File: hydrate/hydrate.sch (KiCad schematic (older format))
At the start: 1 part, among them U1 K32L2Bx1VFM0A

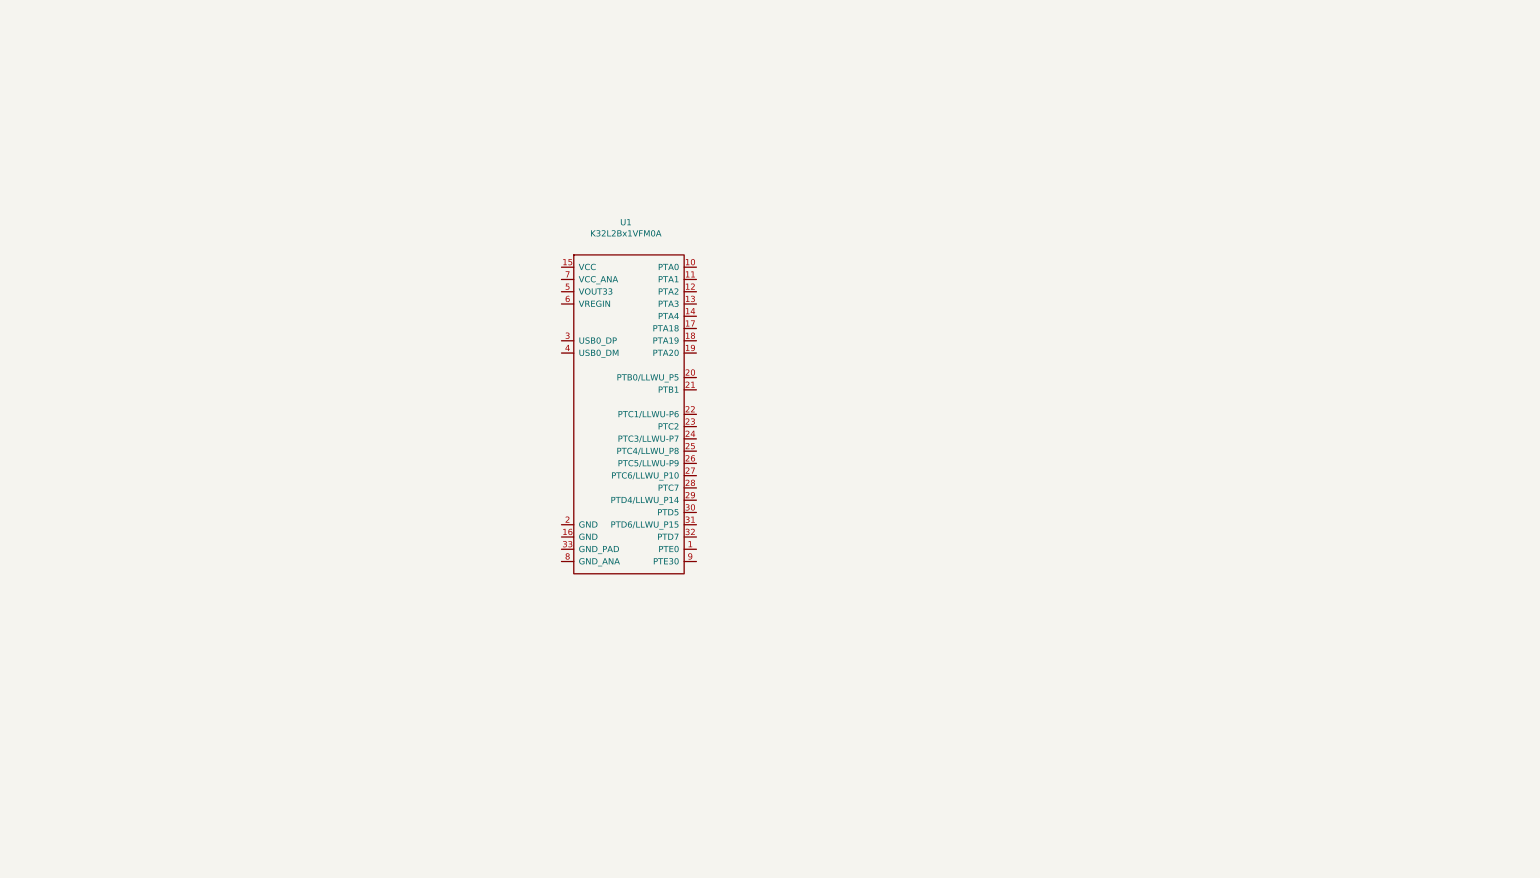
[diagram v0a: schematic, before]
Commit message: Saving place. MCU and power management ICs added
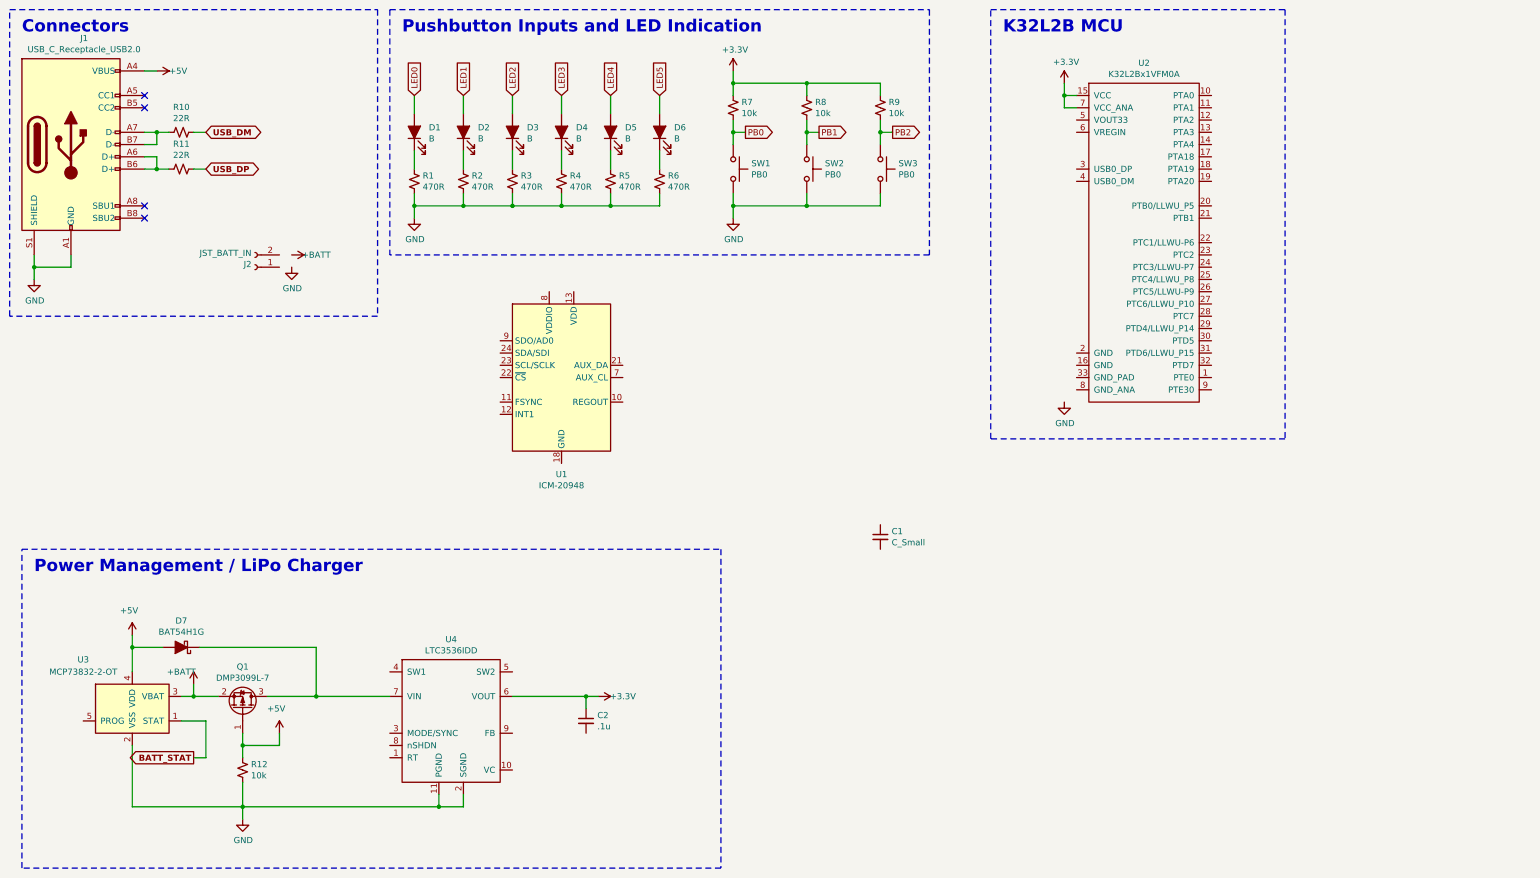
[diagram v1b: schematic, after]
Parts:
- removed U1: K32L2Bx1VFM0A, hydrate:QFN-32_EP_5x5_Pitch0.5mm, symbol hydrate:K32L2Bx1VFM0A
- added C1: C_Small, symbol Device:C_Small
- added C2: .1u, symbol Device:C_Small
- added D1, D2, D3, D4, D5, D6: B, symbol Device:LED_ALT
- added D7: BAT54H1G, symbol Device:D_Schottky_ALT
- added J1: USB_C_Receptacle_USB2.0, symbol Connector:USB_C_Receptacle_USB2.0
- added J2: JST_BATT_IN, symbol Connector:Conn_01x02_Female
- added Q1: DMP3099L-7, Package_TO_SOT_SMD:SOT-23, symbol Transistor_FET:VP0610T
- added R1, R2, R3, R4, R5, R6: 470R, symbol Device:R_Small_US
- added R10, R11: 22R, symbol Device:R_Small_US
- added R12, R7, R8, R9: 10k, symbol Device:R_Small_US
- added SW1, SW2, SW3: PB0, symbol Switch:SW_Push
- added U1: ICM-20948, Sensor_Motion:InvenSense_QFN-24_3x3mm_P0.4mm, symbol Sensor_Motion:ICM-20948
- added U2: K32L2Bx1VFM0A, hydrate:QFN-32_EP_5x5_Pitch0.5mm, symbol hydrate:K32L2Bx1VFM0A
- added U3: MCP73832-2-OT, Package_TO_SOT_SMD:SOT-23-5, symbol Battery_Management:MCP73832-2-OT
- added U4: LTC3536IDD, hydrate:DFN-10-1EP_3x3mm_P0.5mm_EP0.25x0.70mm, symbol hydrate:LTC3536IDD
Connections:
- new net: U1.18 (GND), U1.20 (GND)
- new net: D1.1 (K), R1.1
- new net: J1.A6 (D+), J1.B6 (D+), R11.2
- new net: J1.A7 (D-), J1.B7 (D-), R10.2
- new net: D2.1 (K), R2.1
- new net: D3.1 (K), R3.1
- new net: D4.1 (K), R4.1
- new net: D5.1 (K), R5.1
- new net: D6.1 (K), R6.1
- new net: D7.1 (K), Q1.3 (D), U4.7 (VIN)
- new net +3V3: C2.1, R7.1, R8.1, R9.1, U2.15 (VCC), U2.7 (VCC_ANA), U4.6 (VOUT)
- new net +5V: D7.2 (A), J1.A4 (VBUS), J1.A9 (VBUS), J1.B4 (VBUS), J1.B9 (VBUS), Q1.1 (G), R12.1, U3.4 (VDD)
- new net +BATT: Q1.2 (S), U3.3 (VBAT)
- new net BATT_STAT: U3.1 (STAT)
- new net GND: J1.A1 (GND), J1.A12 (GND), J1.B1 (GND), J1.B12 (GND), J1.S1 (SHIELD), R1.2, R12.2, R2.2, R3.2, R4.2, R5.2, R6.2, SW1.2, SW2.2, SW3.2, U3.2 (VSS), U4.11 (PGND), U4.2 (SGND)
- new net LED0: D1.2 (A)
- new net LED1: D2.2 (A)
- new net LED2: D3.2 (A)
- new net LED3: D4.2 (A)
- new net LED4: D5.2 (A)
- new net LED5: D6.2 (A)
- new net PB0: R7.2, SW1.1
- new net PB1: R8.2, SW2.1
- new net PB2: R9.2, SW3.1
- new net USB_DM: R10.1
- new net USB_DP: R11.1
- no-connect marks 0 -> 4
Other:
- note added: "Connectors"
- note added: "K32L2B MCU"
- note added: "Power Management / LiPo Charger"
- note added: "Pushbutton Inputs and LED Indication"

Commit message: Added LT switcher
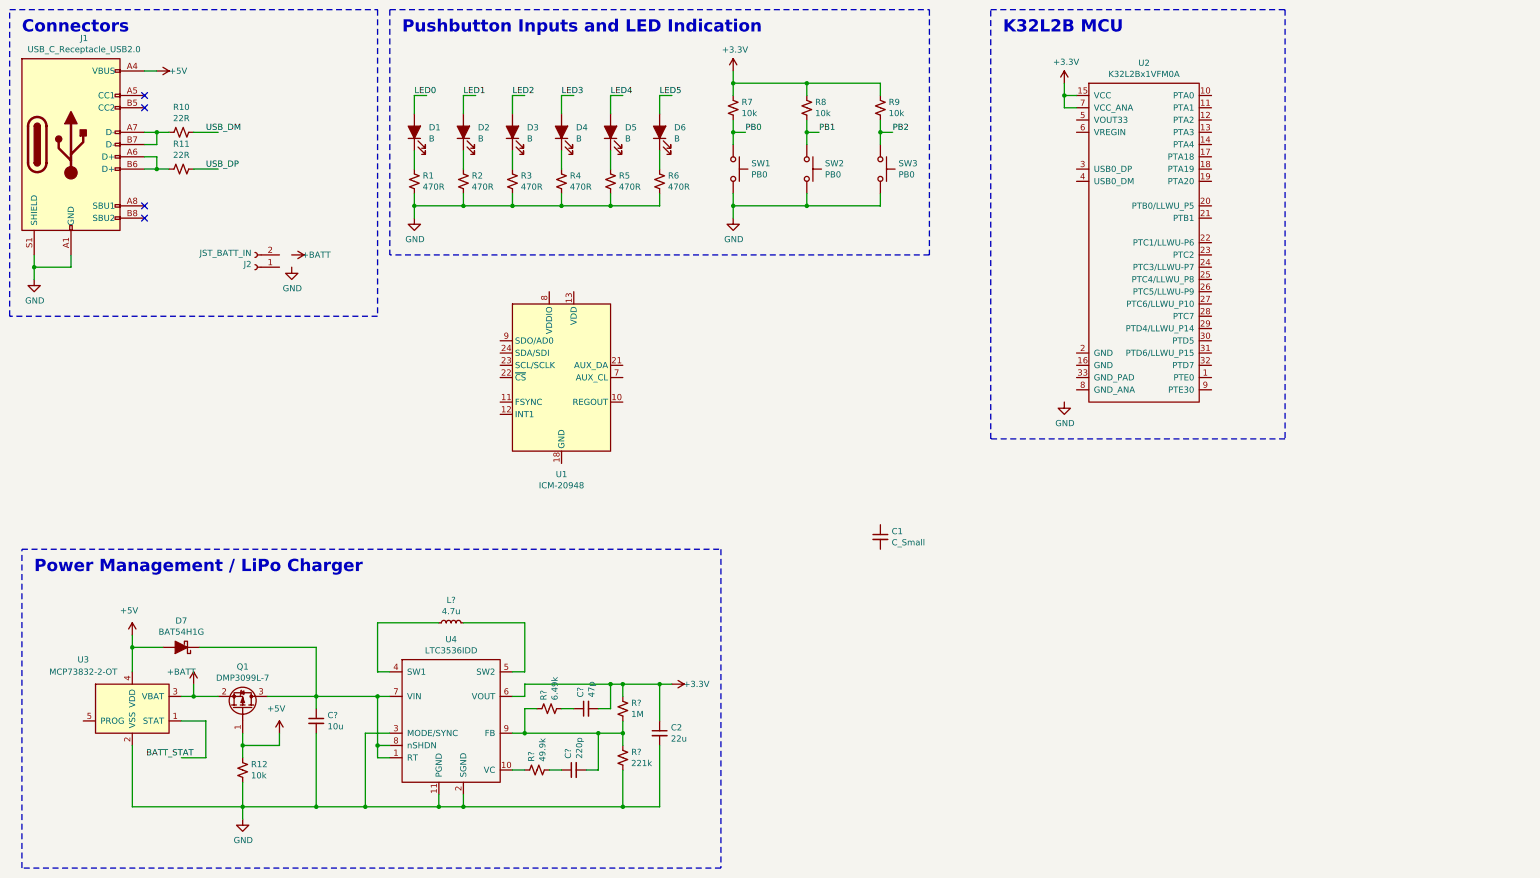
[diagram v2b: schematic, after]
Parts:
- added C?: 10u, symbol Device:C_Small
- added C?: 47p, symbol Device:C_Small
- added C?: 220p, symbol Device:C_Small
- added L?: 4.7u, symbol Device:L_Small
- added R?: 1M, symbol Device:R_Small_US
- added R?: 221k, symbol Device:R_Small_US
- added R?: 6.49k, symbol Device:R_Small_US
- added R?: 49.9k, symbol Device:R_Small_US
- C2: value .1u -> 22u
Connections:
- wire segments 92 -> 138
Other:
- moved on the sheet: C2

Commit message: Began layout of Switcher and Battery charger on backside of board
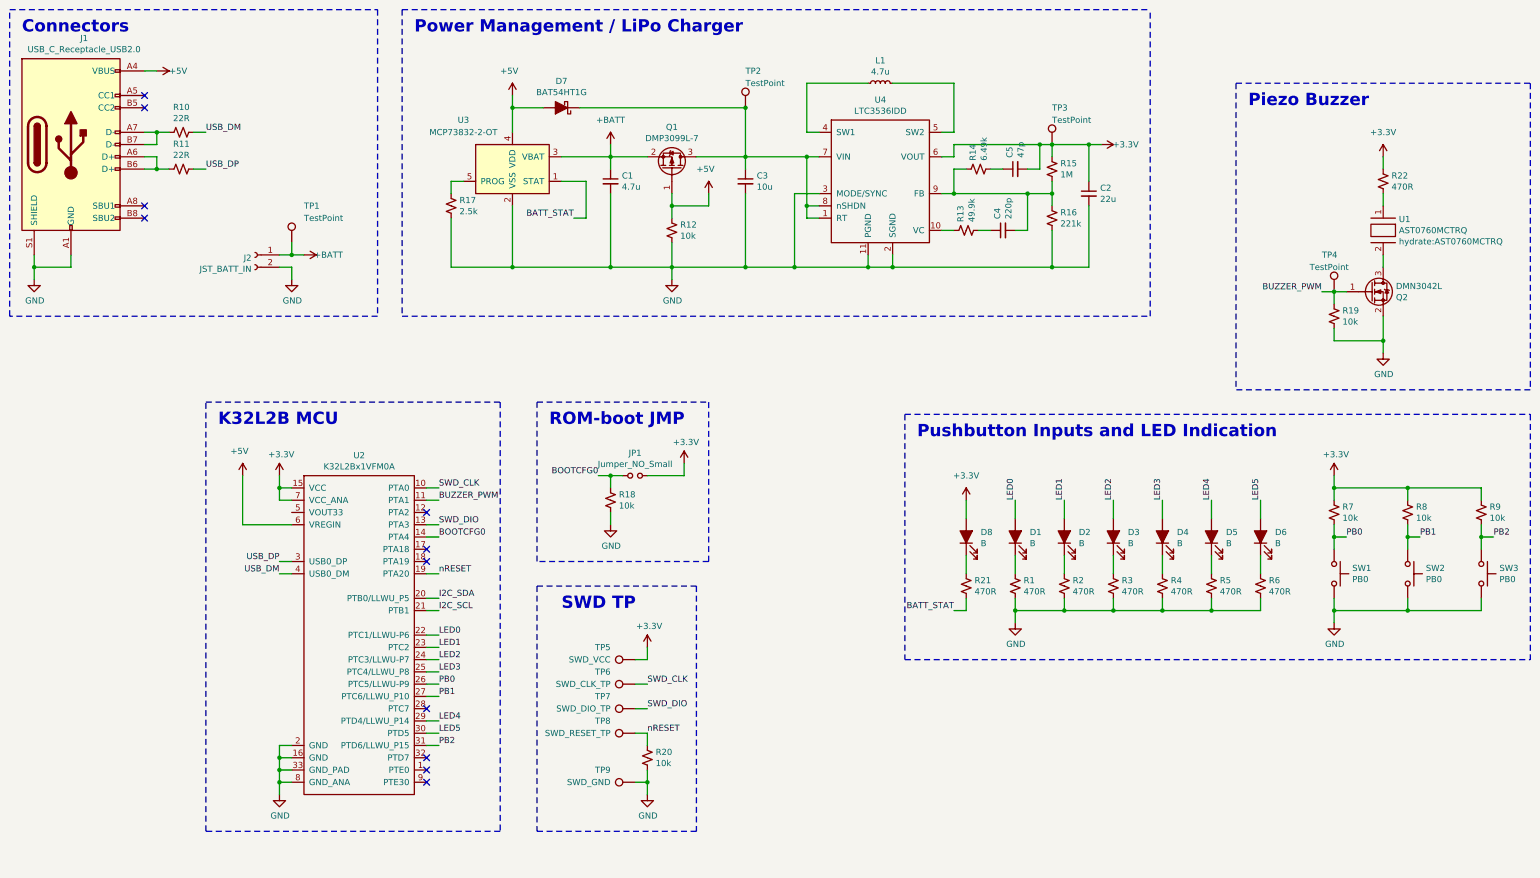
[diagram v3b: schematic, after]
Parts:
- removed U1: ICM-20948, Sensor_Motion:InvenSense_QFN-24_3x3mm_P0.4mm, symbol Sensor_Motion:ICM-20948
- added D8: B, LED_SMD:LED_0402_1005Metric, symbol Device:LED_ALT
- added JP1: Jumper_NO_Small, Jumper:SolderJumper-2_P1.3mm_Open_TrianglePad1.0x1.5mm, symbol Device:Jumper_NO_Small
- added Q2: DMN3042L, Package_TO_SOT_SMD:SOT-23, symbol Transistor_FET:DMN3042L
- added R17: 2.5k, Resistor_SMD:R_0402_1005Metric, symbol Device:R_Small_US
- added R18, R19, R20: 10k, Resistor_SMD:R_0402_1005Metric, symbol Device:R_Small_US
- added R21, R22: 470R, Resistor_SMD:R_0402_1005Metric, symbol Device:R_Small_US
- added TP1, TP2, TP3, TP4: TestPoint, TestPoint:TestPoint_Pad_1.0x1.0mm, symbol Connector:TestPoint
- added TP5: SWD_VCC, TestPoint:TestPoint_Pad_1.5x1.5mm, symbol Connector:TestPoint
- added TP6: SWD_CLK_TP, TestPoint:TestPoint_Pad_1.5x1.5mm, symbol Connector:TestPoint
- added TP7: SWD_DIO_TP, TestPoint:TestPoint_Pad_1.5x1.5mm, symbol Connector:TestPoint
- added TP8: SWD_RESET_TP, TestPoint:TestPoint_Pad_1.5x1.5mm, symbol Connector:TestPoint
- added TP9: SWD_GND, TestPoint:TestPoint_Pad_1.5x1.5mm, symbol Connector:TestPoint
- added U1: AST0760MCTRQ, hydrate:AST0760MCTRQ, symbol hydrate:AST0760MCTRQ
- C1: value C_Small -> 4.7u; footprint (none) -> Capacitor_SMD:C_0402_1005Metric
- C2: footprint (none) -> Capacitor_SMD:C_0402_1005Metric
- C3, C4, C5: renamed from C?; footprint (none) -> Capacitor_SMD:C_0402_1005Metric
- D1, D2, D3, D4, D5, D6: footprint (none) -> LED_SMD:LED_0402_1005Metric
- D7: value BAT54H1G -> BAT54HT1G; footprint (none) -> Diode_SMD:D_SOD-323
- J1: footprint (none) -> Connector_USB:USB_C_Receptacle_GCT_USB4085
- J2: footprint (none) -> Connector_JST:JST_PH_S2B-PH-SM4-TB_1x02-1MP_P2.00mm_Horizontal
- L1: renamed from L?; footprint (none) -> Capacitor_SMD:C_0402_1005Metric
- R1, R10, R11, R12, R2, R3, R4, R5, R6, R7, R8, R9: footprint (none) -> Resistor_SMD:R_0402_1005Metric
- R13, R14, R15, R16: renamed from R?; footprint (none) -> Resistor_SMD:R_0402_1005Metric
- SW1, SW2, SW3: footprint (none) -> Button_Switch_SMD:Panasonic_EVQPUL_EVQPUC
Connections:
- net labels added: BOOTCFG0, BUZZER_PWM, I2C_SCL, I2C_SDA, SWD_CLK, SWD_DIO, nRESET
- wire segments 138 -> 201
- no-connect marks 4 -> 11
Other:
- note added: "Piezo Buzzer"
- note added: "ROM-boot JMP"
- note added: "SWD TP"
- moved on the sheet: C2, C3, C4, C5, D1, D2, D3, D4, D5, D6, D7, L1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
